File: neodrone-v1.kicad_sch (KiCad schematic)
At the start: 0 parts

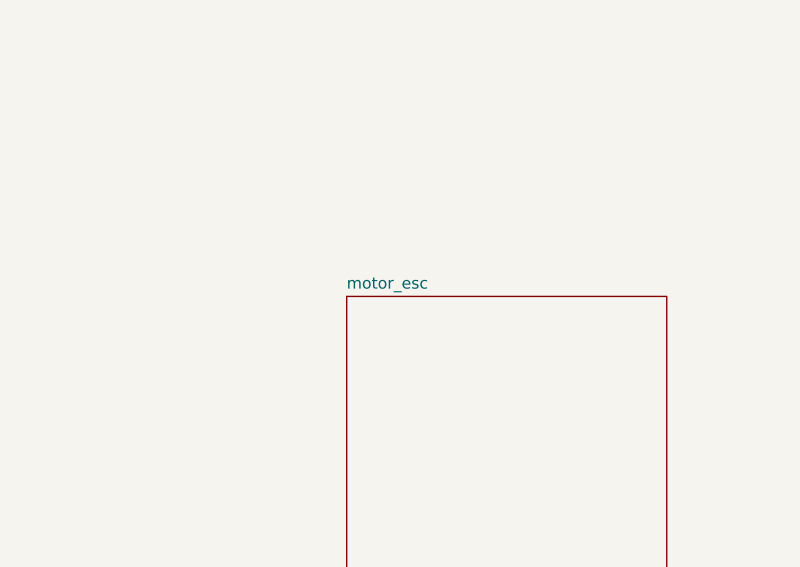
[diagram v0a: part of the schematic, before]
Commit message: more esc schematics, refactoring, root schematic edits
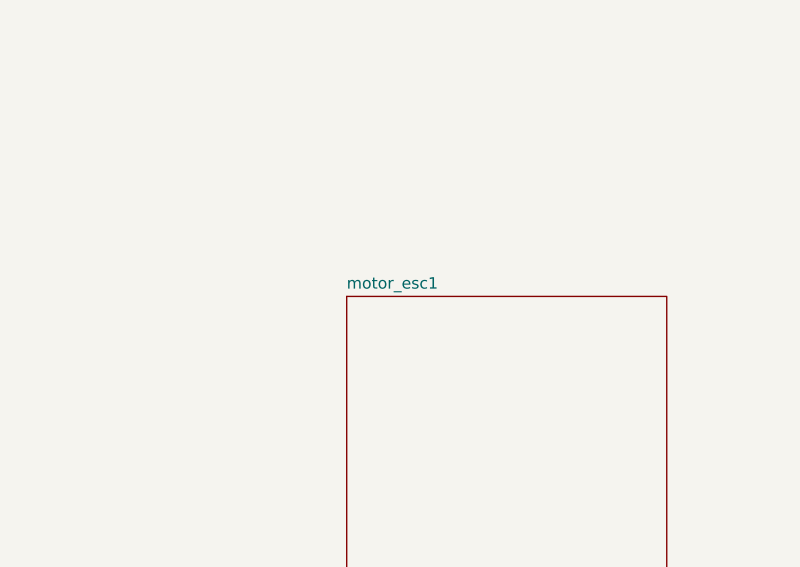
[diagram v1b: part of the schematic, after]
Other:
- sheet motor_esc renamed motor_esc1
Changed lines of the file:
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@@
 			(color 0 0 0 0.0000)
 		)
-		(property "Sheetname" "motor_esc"
+		(property "Sheetname" "motor_esc1"
 			(at 228.6 97.0784 0)
 			(effects

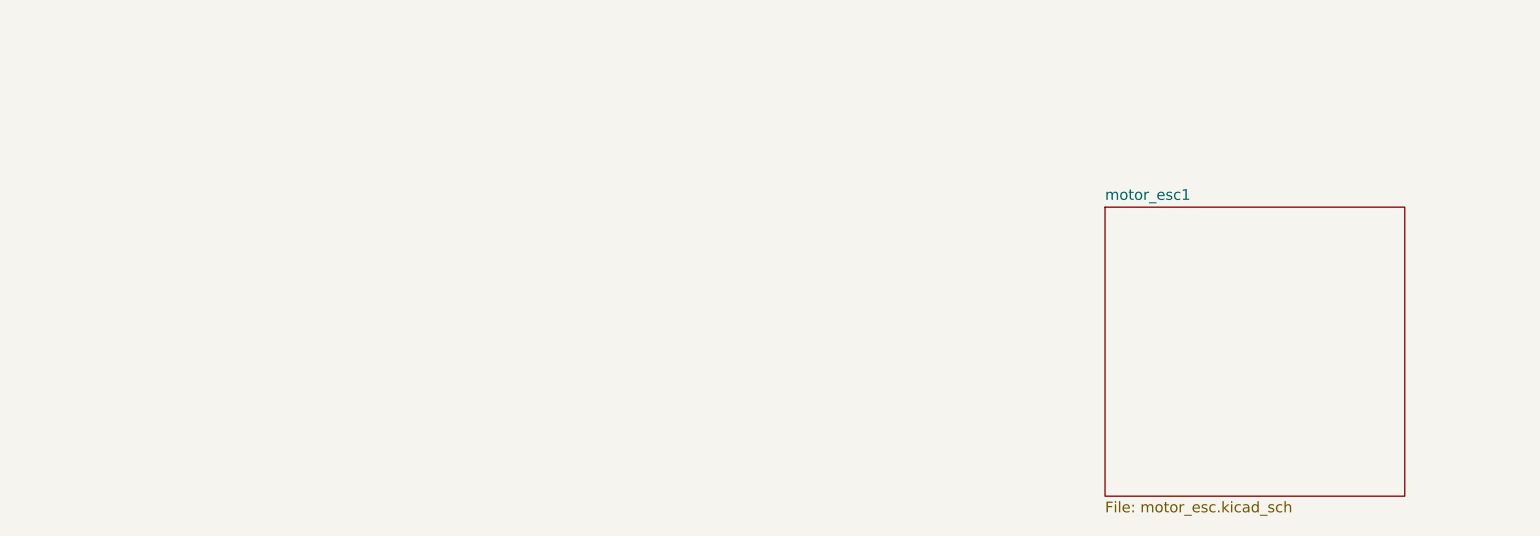
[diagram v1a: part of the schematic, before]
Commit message: Schematics mostly done, netclasses, coords for esc (angled)
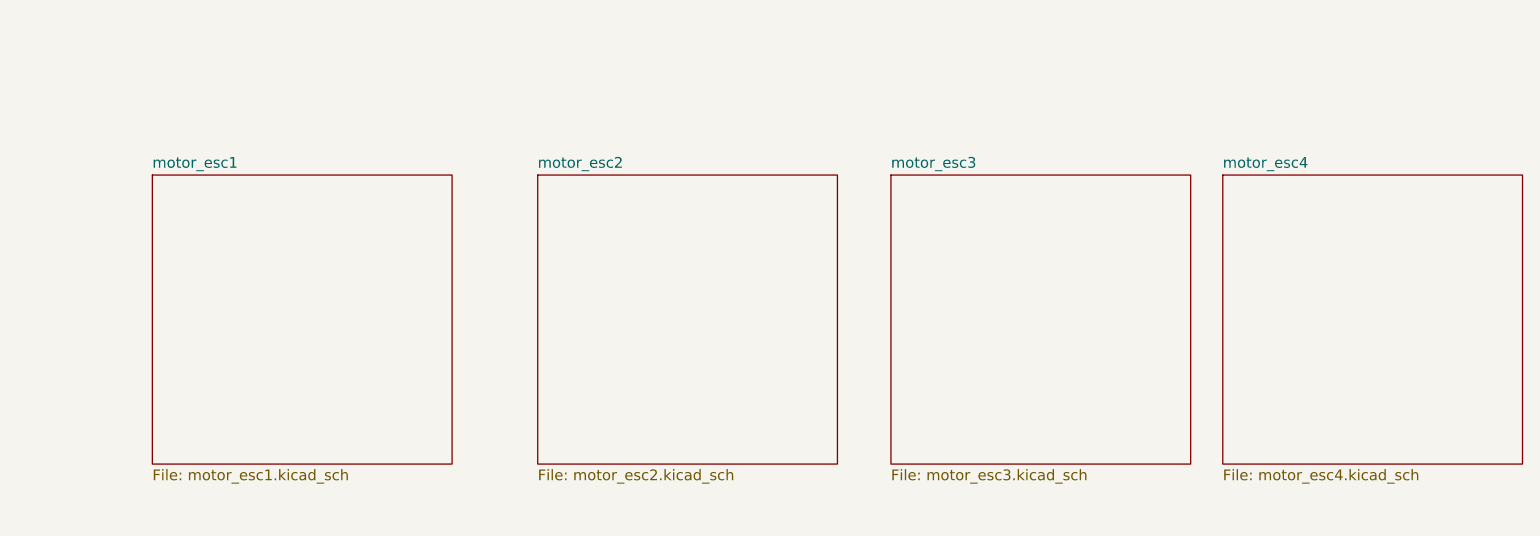
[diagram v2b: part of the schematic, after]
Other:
- added sheet motor_esc2 (motor_esc2.kicad_sch)
- added sheet motor_esc3 (motor_esc3.kicad_sch)
- added sheet motor_esc4 (motor_esc4.kicad_sch)
- sheet motor_esc1: file motor_esc.kicad_sch -> motor_esc1.kicad_sch
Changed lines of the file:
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@@
+	)
+	(sheet
+		(at 161.29 93.98)
+		(size 35.56 34.29)
+		(exclude_from_sim no)
+		(in_bom yes)
+		(on_board yes)
+		(dnp no)
+		(fields_autoplaced yes)
+		(stroke
+			(width 0.1524)
+			(type solid)
+		)
+		(fill
+			(color 0 0 0 0.0000)
+		)
+		(property "Sheetname" "motor_esc2"
+			(at 161.29 93.2684 0)
+			(effects
+				(font
+					(size 1.27 1.27)
+				)
+				(justify left bottom)
+			)
+		)
+		(property "Sheetfile" "motor_esc2.kicad_sch"
+			(at 161.29 128.8546 0)
+			(effects
+				(font
+					(size 1.27 1.27)
+				)
+				(justify left top)
+			)
+		)
+		(instances
+			(project "neodrone-v1"
+				(path "/ec430d83-72cd-4950-a197-fb5338d7c552"
+					(page "6")
+				)
+			)
+		)
 	)
 	(sheet
@@
 				(path "/ec430d83-72cd-4950-a197-fb5338d7c552"
 					(page "4")
+				)
+			)
+		)
+	)
+	(sheet
+		(at 242.57 93.98)
+		(size 35.56 34.29)
+		(exclude_from_sim no)
+		(in_bom yes)
+		(on_board yes)
+		(dnp no)
+		(fields_autoplaced yes)
+		(stroke
+			(width 0.1524)
+			(type solid)
+		)
+		(fill
+			(color 0 0 0 0.0000)
+		)
+		(property "Sheetname" "motor_esc4"
+			(at 242.57 93.2684 0)
+			(effects
+				(font
+					(size 1.27 1.27)
+				)
+				(justify left bottom)
+			)
+		)
+		(property "Sheetfile" "motor_esc4.kicad_sch"
+			(at 242.57 128.8546 0)
+			(effects
+				(font
+					(size 1.27 1.27)
+				)
+				(justify left top)
+			)
+		)
+		(instances
+			(project "neodrone-v1"
+				(path "/ec430d83-72cd-4950-a197-fb5338d7c552"
+					(page "8")
 				)
 			)
@@
 	)
 	(sheet
+		(at 203.2 93.98)
+		(size 35.56 34.29)
+		(exclude_from_sim no)
+		(in_bom yes)
+		(on_board yes)
+		(dnp no)
+		(fields_autoplaced yes)
+		(stroke
+			(width 0.1524)
+			(type solid)
+		)
+		(fill
+			(color 0 0 0 0.0000)
+		)
+		(property "Sheetname" "motor_esc3"
+			(at 203.2 93.2684 0)
+			(effects
+				(font
+					(size 1.27 1.27)
+				)
+				(justify left bottom)
+			)
+		)
+		(property "Sheetfile" "motor_esc3.kicad_sch"
+			(at 203.2 128.8546 0)
+			(effects
+				(font
+					(size 1.27 1.27)
+				)
+				(justify left top)
+			)
+		)
+		(instances
+			(project "neodrone-v1"
+				(path "/ec430d83-72cd-4950-a197-fb5338d7c552"
+					(page "7")
+				)
+			)
+		)
+	)
+	(sheet
 		(at 114.3 22.86)
 		(size 35.56 29.21)
@@
 	)
 	(sheet
-		(at 228.6 97.79)
+		(at 115.57 93.98)
 		(size 35.56 34.29)
 		(exclude_from_sim no)
@@
 		)
 		(property "Sheetname" "motor_esc1"
-			(at 228.6 97.0784 0)
-			(effects
-				(font
-					(size 1.27 1.27)
-				)
-				(justify left bottom)
-			)
-		)
-		(property "Sheetfile" "motor_esc.kicad_sch"
-			(at 228.6 132.6646 0)
+			(at 115.57 93.2684 0)
+			(effects
+				(font
+					(size 1.27 1.27)
+				)
+				(justify left bottom)
+			)
+		)
+		(property "Sheetfile" "motor_esc1.kicad_sch"
+			(at 115.57 128.8546 0)
 			(effects
 				(font
@@
 			(project "neodrone-v1"
 				(path "/ec430d83-72cd-4950-a197-fb5338d7c552"
-					(page "6")
-				)
-			)
+					(page "9")
+				)
+			)
